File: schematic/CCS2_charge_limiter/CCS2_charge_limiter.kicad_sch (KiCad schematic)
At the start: 22 parts, among them J1 Conn_01x02, Q2 AO3400, U1 LM393, U2 SFH617A-3, U3 SFH617A-3, U4 SFH617A-3

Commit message: Update VSCode, docs, platformio and schematic
Add VSCode extension recommendations (esp-decoder, pioarduino) and tidy extensions.json. Update CLAUDE.md with hand-verified CP sensing values and note tightening of resistor tolerances. Change PlatformIO OTA upload_port to 192.168.0.151. Mark three schematic resistor symbols with a 1% "Tolerance" property to reflect tightened R1/R2/R3 values and close the A/B threshold margin.
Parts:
- R1, R2, R3: Tolerance (none) -> 1%
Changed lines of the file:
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@@
+			)
+		)
+		(property "Tolerance" "1%"
+			(at 67.31 50.8 0)
+			(hide yes)
+			(show_name no)
+			(do_not_autoplace no)
+			(effects
+				(font
+					(size 1.27 1.27)
+				)
 			)
 		)
@@
 			)
 		)
+		(property "Tolerance" "1%"
+			(at 33.02 71.12 0)
+			(hide yes)
+			(show_name no)
+			(do_not_autoplace no)
+			(effects
+				(font
+					(size 1.27 1.27)
+				)
+			)
+		)
 		(pin "1"
 		)
@@
 			(at 33.02 60.96 0)
 			(hide yes)
+			(show_name no)
+			(do_not_autoplace no)
+			(effects
+				(font
+					(size 1.27 1.27)
+				)
+			)
+		)
+		(property "Tolerance" "1%"
+			(at 33.02 60.96 0)
+			(hide yes)

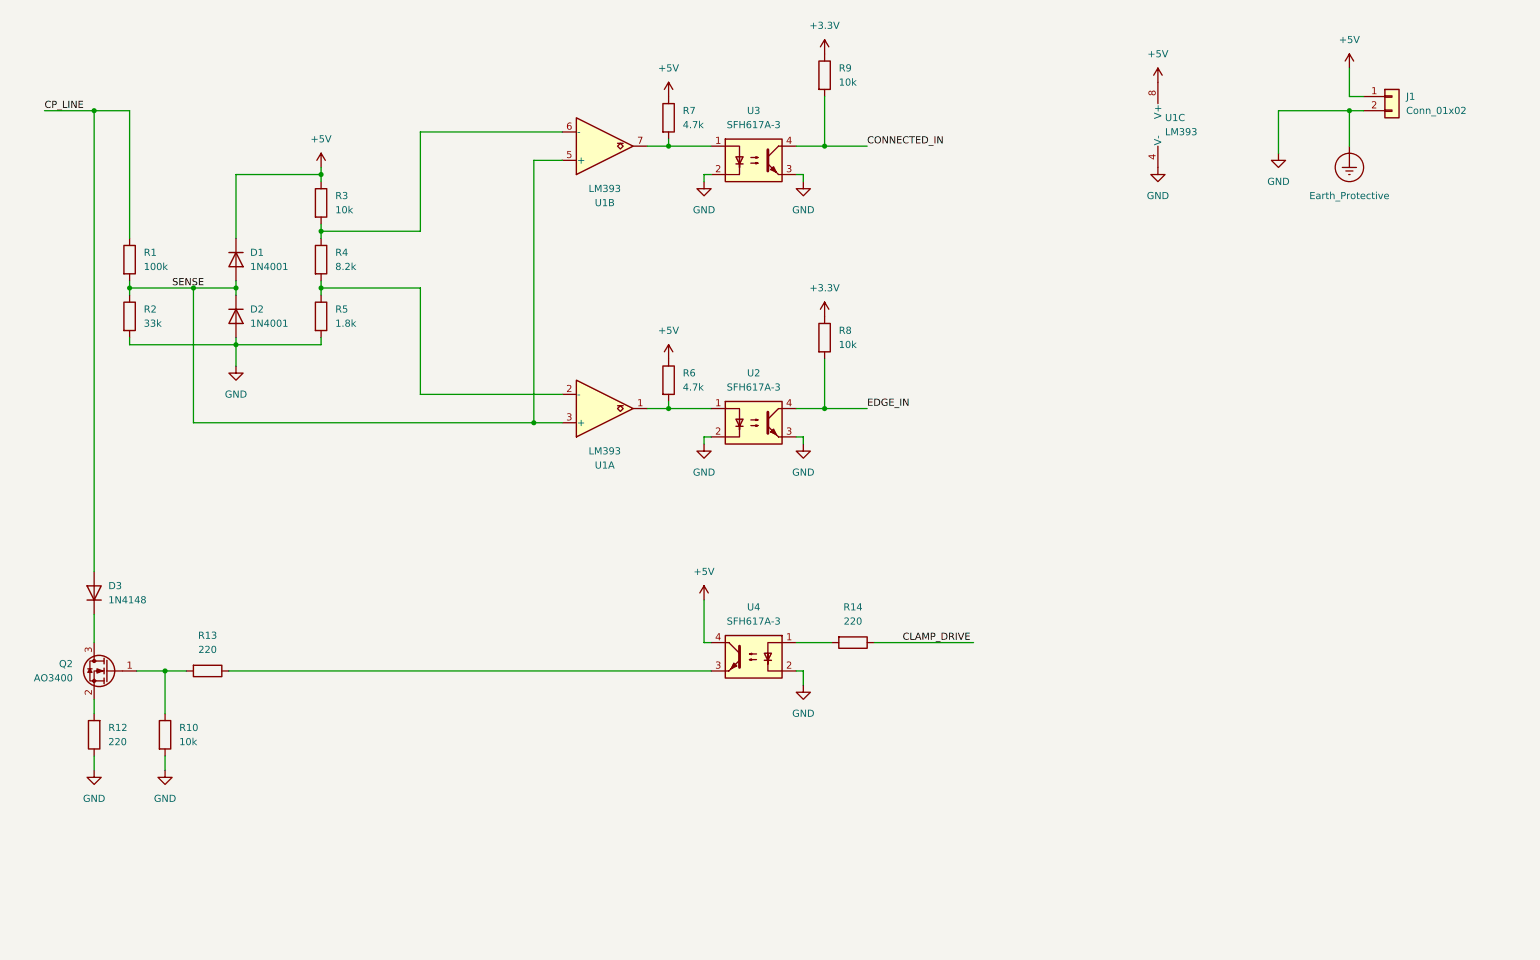
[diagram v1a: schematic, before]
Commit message: Add CP disconnect relay and relay-control logic
Introduce a normally-closed CP disconnect relay and firmware support so CP_STANDBY isolates the vehicle (opens relay) when surplus is genuinely below the 6A floor. MODE_BYPASS/stale-data keeps the relay closed. Added CP_DISCONNECT_RELAY_GPIO and RELAY_MIN_DWELL_MS to config.h, initialized and driven in cp_interceptor.cpp, with dwell-time guarding to avoid relay chatter. Updated docs (CLAUDE.md, README.md), KiCad schematic (kicad_pro/.kicad_sch and schematic.png), and UI strings (solar_control.cpp, status_display.cpp). Minor shared_state comments updated to reflect semantics.
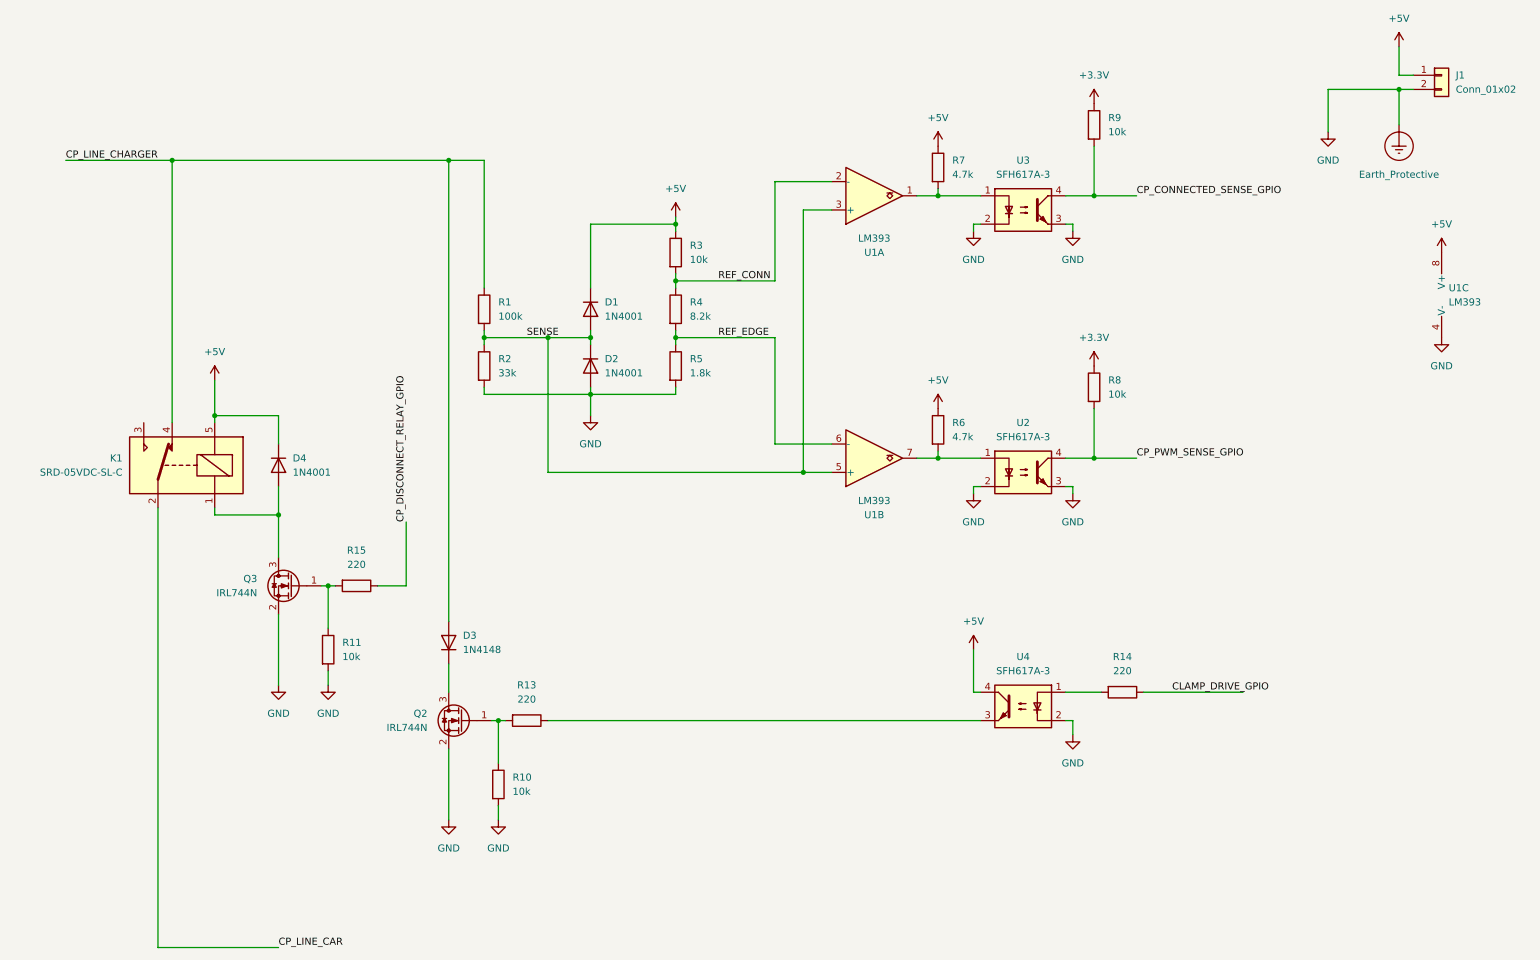
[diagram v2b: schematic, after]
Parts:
- removed R12: 220, symbol Device:R
- added D4: 1N4001, symbol Device:D
- added K1: SRD-05VDC-SL-C, Relay_THT:Relay_SPDT_SANYOU_SRD_Series_Form_C, symbol Relay:G5Q-1
- added Q3: IRL744N, Package_TO_SOT_SMD:SOT-23, symbol Transistor_FET:Q_NMOS_GSD
- added R11: 10k, symbol Device:R
- added R15: 220, symbol Device:R
- Q2: value AO3400 -> IRL744N; Notes (none) -> Overkill but it's what I have
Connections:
- net +5V: now also D4.1 (K), K1.5
- net Earth_Protective: now also Q2.2 (S), Q3.2 (S), R11.2
- net at R6.2, U2.1: now also U1.7; no longer U1.1
- net REF_CONN: now reaches R3.2, R4.1
- net REF_CONN: now also U1.2 (-); no longer U1.6 (-)
- net at R7.2, U3.1: now also U1.1; no longer U1.7
- net REF_EDGE: now reaches R4.2, R5.1
- net REF_EDGE: now also U1.6 (-); no longer U1.2 (-)
- net CLAMP_DRIVE renamed CLAMP_DRIVE_GPIO
- net CONNECTED_IN renamed CP_CONNECTED_SENSE_GPIO
- net CP_LINE renamed CP_LINE_CHARGER
- net CP_LINE_CHARGER: now also K1.4
- net EDGE_IN renamed CP_PWM_SENSE_GPIO
- new net: Q3.1 (G), R11.1, R15.2
- new net: D4.2 (A), K1.1, Q3.3 (D)
- new net CP_DISCONNECT_RELAY_GPIO: R15.1
- new net CP_LINE_CAR: K1.2
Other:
- title: (none) -> CCS2 CP Interceptor
- moved on the sheet: D1, D2, D3, J1, Q2, R1, R10, R13, R14, R2, R3, R4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
